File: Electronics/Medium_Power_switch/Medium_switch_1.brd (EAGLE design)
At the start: 40 x 19 mm, 37 parts, among them U1 BTS700151ESPXUMA1, U2 AP63205WU-7

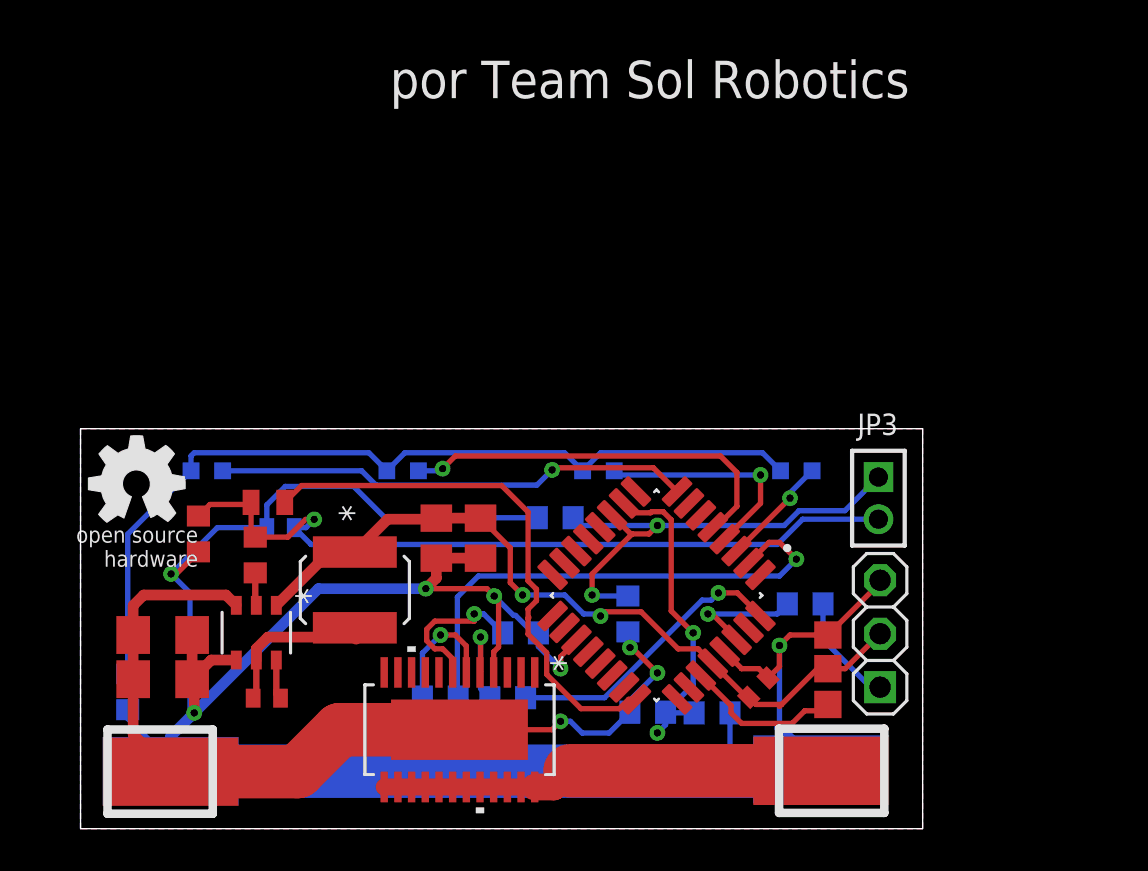
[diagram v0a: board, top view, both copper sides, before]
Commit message: Nuevos esquematicos y PCB
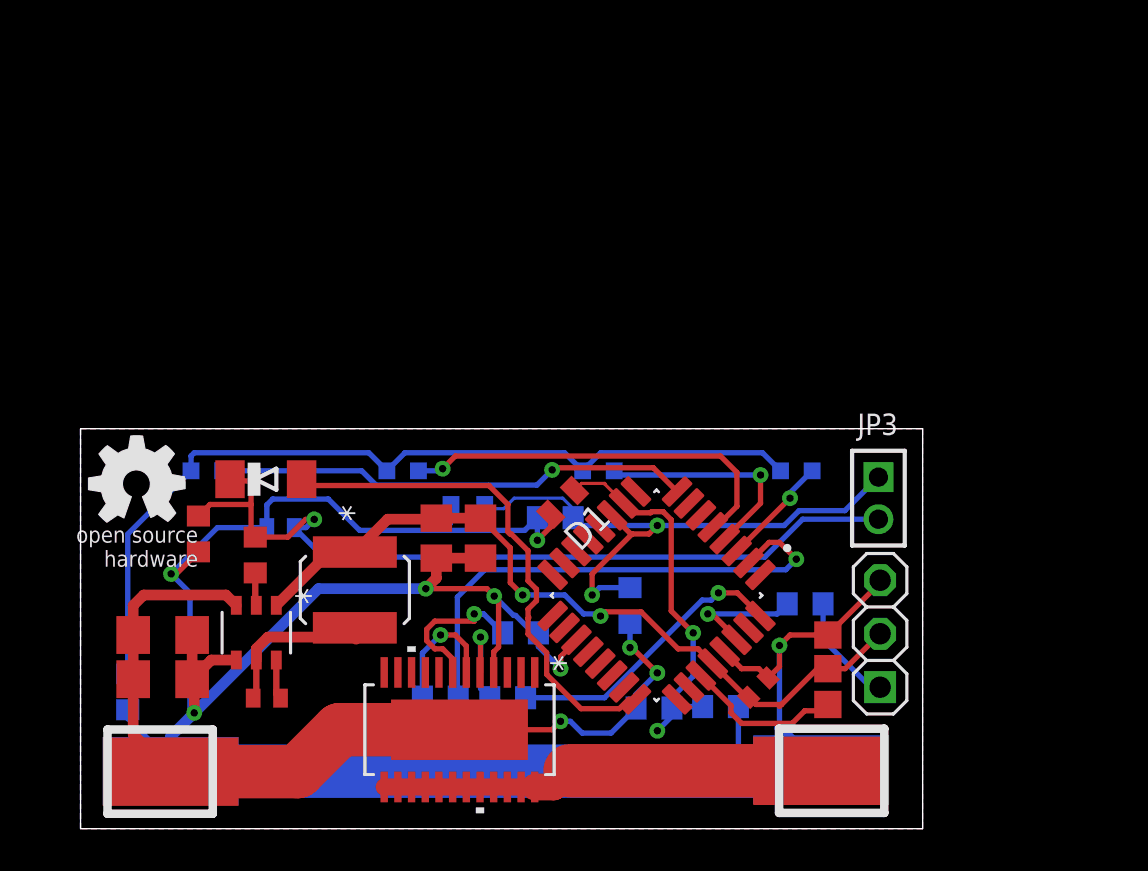
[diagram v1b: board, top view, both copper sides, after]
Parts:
- added D1, D3: (no value), diode:MICROMELF-R
- D2: device diode:MICROMELF-R -> diode:MINIMELF
- RBAT1, RESV+: value (none) -> 23k
- RBAT2, RBAT4, RBAT5, RCH2: value (none) -> 10k
- RBAT3, RCH1, RDIAGEN, RPWREN: value (none) -> 1.2k
- moved D2 1.10 mm to (8.80, 16.6)
- moved RBAT4 0.50 mm to (30.4, 5.80)
- moved RESV+ 0.41 mm to (26.1, 10.6)
- moved RBAT1 0.36 mm to (27.2, 5.73)
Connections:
- net BOTON: now also D3.C
- net GND: now also D1.A, D3.A
- net N$11: now also D1.C
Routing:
- net BOTON: track 23.7 -> 29.0 mm
- net GND: track 124.7 -> 128.9 mm, vias 6 -> 7
- net N$11: track 15.2 -> 18.2 mm
- net REG_ON: track 37.3 -> 39.8 mm
- net N$5: track 26.0 -> 24.9 mm
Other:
- board text removed: "Por xDzohlx"
- board text removed: "por Team Sol Robotics"
